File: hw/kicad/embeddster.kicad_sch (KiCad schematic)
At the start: 1 part, among them U1 ESP32-DEVKIT-V1

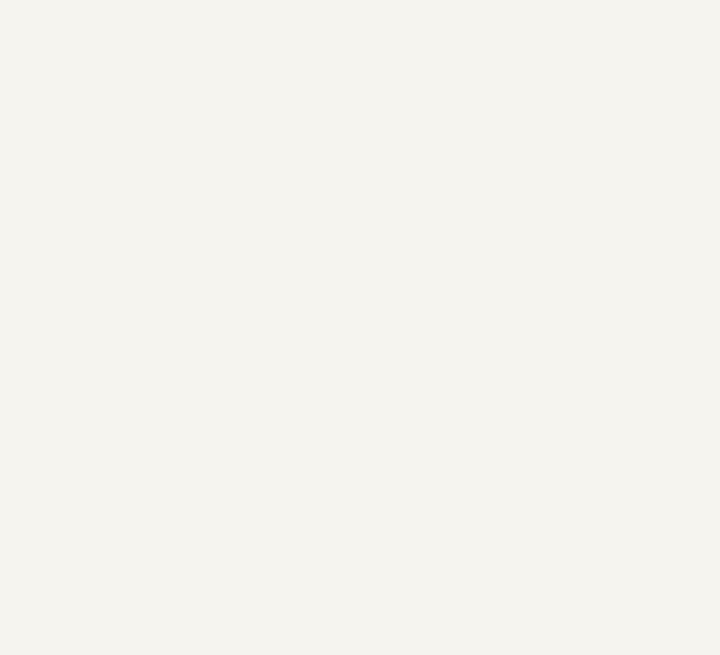
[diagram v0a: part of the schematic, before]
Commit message: Add custom KiCad symbol&footproint for PLACA_CAN_V20190517
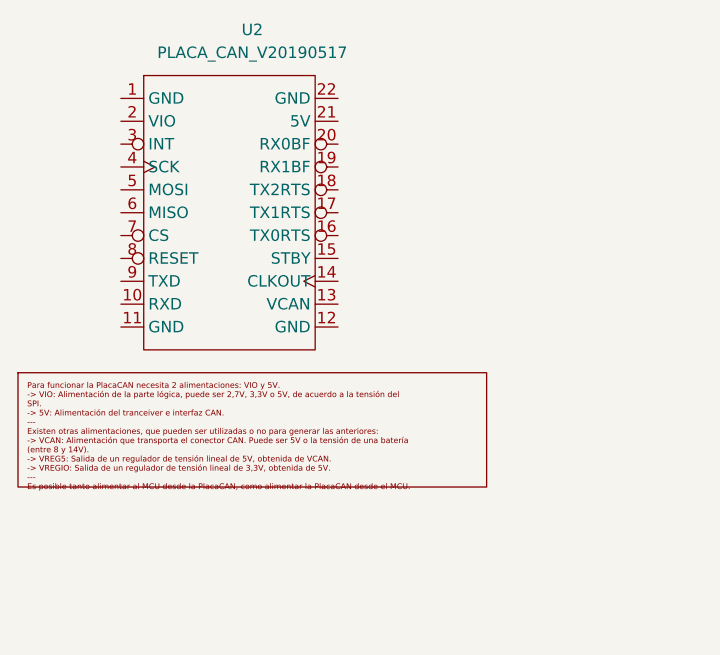
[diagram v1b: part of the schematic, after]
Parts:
- added U2: PLACA_CAN_V20190517, PLACA_CAN_V20190517:PLACA_CAN_V20190517, symbol PLACA_CAN_V20190517:PLACA_CAN_V20190517
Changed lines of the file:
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@@
+		)
+	)
+	(symbol
+		(lib_id "PLACA_CAN_V20190517:PLACA_CAN_V20190517")
+		(at 57.15 27.94 0)
+		(unit 1)
+		(exclude_from_sim no)
+		(in_bom yes)
+		(on_board yes)
+		(dnp no)
+		(fields_autoplaced yes)
+		(property "Reference" "U2"
+			(at 59.055 24.13 0)
+			(effects
+				(font
+					(size 1.27 1.27)
+				)
+			)
+		)
+		(property "Value" "PLACA_CAN_V20190517"
+			(at 59.055 26.67 0)
+			(effects
+				(font
+					(size 1.27 1.27)
+				)
+			)
+		)
+		(property "Footprint" "PLACA_CAN_V20190517:PLACA_CAN_V20190517"
+			(at 57.15 27.94 0)
+			(effects
+				(font
+					(size 1.27 1.27)
+				)
+				(hide yes)
+			)
+		)
+		(property "Datasheet" ""
+			(at 57.15 27.94 0)
+			(effects
+				(font
+					(size 1.27 1.27)
+				)
+				(hide yes)
+			)
+		)
+		(property "Description" ""
+			(at 57.15 27.94 0)
+			(effects
+				(font
+					(size 1.27 1.27)
+				)
+				(hide yes)
+			)
+		)
+		(pin "7"
+		)
+		(pin "20"
+		)
+		(pin "19"
+		)
+		(pin "21"
+		)
+		(pin "2"
+		)
+		(pin "4"
+		)
+		(pin "13"
+		)
+		(pin "22"
+		)
+		(pin "17"
+		)
+		(pin "1"
+		)
+		(pin "5"
+		)
+		(pin "18"
+		)
+		(pin "15"
+		)
+		(pin "16"
+		)
+		(pin "3"
+		)
+		(pin "14"
+		)
+		(pin "6"
+		)
+		(pin "11"
+		)
+		(pin "8"
+		)
+		(pin "10"
+		)
+		(pin "9"
+		)
+		(pin "12"
+		)
+		(instances
+			(project ""
+				(path "/ce96a9a7-c6cd-448d-a47b-e48e55834808"
+					(reference "U2")
+					(unit 1)
+				)
+			)
 		)
 	)

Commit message: sch supporting tp1 & tp2
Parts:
- removed U2: PLACA_CAN_V20190517, PLACA_CAN_V20190517:PLACA_CAN_V20190517, symbol PLACA_CAN_V20190517:PLACA_CAN_V20190517
- added C1, C2: 100n, Capacitor_SMD:C_0805_2012Metric_Pad1.18x1.45mm_HandSolder, symbol Device:C
- added D1, D2, D3, D4, D5, D6: LED, LED_SMD:LED_0805_2012Metric_Pad1.15x1.40mm_HandSolder, symbol Device:LED
- added J1, J2, J3: Conn_01x03_Pin, Connector_PinHeader_2.54mm:PinHeader_1x03_P2.54mm_Vertical, symbol Connector:Conn_01x03_Pin
- added J4: TP1_CONN, Connector_PinSocket_2.54mm:PinSocket_2x09_P2.54mm_Vertical, symbol Connector_Generic:Conn_02x09_Odd_Even
- added JP1, JP2: Jumper_2_Open, TestPoint:TestPoint_2Pads_Pitch2.54mm_Drill0.8mm, symbol Jumper:Jumper_2_Open
- added R1: 680, Resistor_SMD:R_0805_2012Metric_Pad1.20x1.40mm_HandSolder, symbol Device:R
- added R2: 470, Resistor_SMD:R_0805_2012Metric_Pad1.20x1.40mm_HandSolder, symbol Device:R
- added R3, R4, R5, R6: 220, Resistor_SMD:R_0805_2012Metric_Pad1.20x1.40mm_HandSolder, symbol Device:R
- added U1: PLACA_CAN_V20190517, PLACA_CAN_V20190517:PLACA_CAN_V20190517, symbol PLACA_CAN_V20190517:PLACA_CAN_V20190517
- added U3, U4: 74HC595, Package_SO:SOIC-16_3.9x9.9mm_P1.27mm, symbol 74xx:74HC595
- renumbered U1 to U2
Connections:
- net at U2.1 (3V3): now also JP2.1 (A)
- net CAN_MISO: now reaches U2.10 (D19)
- net CAN_MISO: now also U1.6 (MISO)
- net CAN_MOSI: now reaches U2.15 (D23)
- net CAN_MOSI: now also U1.5 (MOSI)
- net GND: now reaches U2.2 (GND), U2.29 (GND)
- net GND: now also C1.1, C2.1, J1.1 (Pin_1), J1.2 (Pin_2), J1.3 (Pin_3), J4.16 (Pin_16), J4.18 (Pin_18), R1.2, R2.2, R3.2, R4.2, R5.2, R6.2, U1.1 (GND), U1.11 (GND), U1.12 (GND), U1.22 (GND), U3.8 (GND), U4.8 (GND)
- net at U2.30 (VIN): now also JP1.2 (B)
- net CAN_nINT: now reaches U2.7 (TX2)
- net CAN_nINT: now also U1.3 (INT)
- net CAN_nCS: now reaches U2.8 (D5)
- net CAN_nCS: now also U1.7 (CS)
- net CAN_SCK: now reaches U2.9 (D18)
- net CAN_SCK: now also U1.4 (SCK)
- new net: D6.2 (A), U4.4 (QE)
- new net: D5.2 (A), U4.5 (QF)
- new net: D4.2 (A), U4.6 (QG)
- new net: D3.2 (A), U4.7 (QH)
- new net: D1.1 (K), R1.1
- new net: D2.1 (K), R2.1
- new net: D6.1 (K), R6.1
- new net: D3.1 (K), R3.1
- new net: D4.1 (K), R4.1
- new net: D5.1 (K), R5.1
- new net +3V3: C1.2, C2.2, D2.2 (A), J3.1 (Pin_1), J3.2 (Pin_2), J3.3 (Pin_3), J4.17 (Pin_17), JP2.2 (B), U3.16 (VCC), U4.16 (VCC)
- new net +5V: D1.2 (A), J2.1 (Pin_1), J2.2 (Pin_2), J2.3 (Pin_3), JP1.1 (A), U1.21 (5V)
- new net 595_LATCH_CLK: U3.12 (RCLK), U4.12 (RCLK)
- new net 595_LINK: U3.9 (QH'), U4.14 (SER)
- new net 595_SHIFT_CLK: U3.11 (SRCLK), U4.11 (SRCLK)
- new net 595_SI: U3.14 (SER)
- new net 595_nOE: U3.13 (~{OE}), U4.13 (~{OE})
- new net 595_nRST: U3.10 (~{SRCLR}), U4.10 (~{SRCLR})
- new net TP1_CSEGA: J4.1 (Pin_1), U3.15 (QA)
- new net TP1_CSEGB: J4.3 (Pin_3), U3.1 (QB)
- new net TP1_CSEGC: J4.5 (Pin_5), U3.2 (QC)
- new net TP1_CSEGD: J4.7 (Pin_7), U3.3 (QD)
- new net TP1_CSEGDP: J4.15 (Pin_15), U3.7 (QH)
- new net TP1_CSEGE: J4.9 (Pin_9), U3.4 (QE)
- new net TP1_CSEGF: J4.11 (Pin_11), U3.5 (QF)
- new net TP1_CSEGG: J4.13 (Pin_13), U3.6 (QG)
- new net TP1_RCHA: J4.6 (Pin_6)
- new net TP1_RCHB: J4.8 (Pin_8)
- new net TP1_RSWITCH: J4.10 (Pin_10)
- new net TP1_SEL0: J4.2 (Pin_2), U4.15 (QA)
- new net TP1_SEL1: J4.4 (Pin_4), U4.1 (QB)
- new net TP1_STATUS0: J4.12 (Pin_12), U4.2 (QC)
- new net TP1_STATUS1: J4.14 (Pin_14), U4.3 (QD)
- no-connect marks 0 -> 13
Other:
- moved on the sheet: U2

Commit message: pcb ready for fab
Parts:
- added C3, C4, C5: 100n, Capacitor_SMD:C_0805_2012Metric_Pad1.18x1.45mm_HandSolder, symbol Device:C
- added J5, J6, J7: Conn_01x05_Socket, Connector_PinSocket_2.54mm:PinSocket_1x05_P2.54mm_Vertical, symbol Connector:Conn_01x05_Socket
- added R7, R8: 10k, Resistor_SMD:R_0805_2012Metric_Pad1.20x1.40mm_HandSolder, symbol Device:R
- D1: footprint LED_SMD:LED_0805_2012Metric_Pad1.15x1.40mm_HandSolder -> LED_THT:LED_D3.0mm
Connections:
- net +3V3: now also U1.2 (VIO), C3.2, R7.1, R8.1
- net 595_LATCH_CLK: now also U2.22 (D33)
- net 595_SHIFT_CLK: now also U2.25 (D27)
- net 595_SI: now also U2.21 (D32)
- net 595_nOE: now also U2.23 (D25), R7.2
- net 595_nRST: now also U2.24 (D26), R8.2
- net GND: now also C3.1, C4.1, C5.1, J5.1 (Pin_1), J5.2 (Pin_2), J5.3 (Pin_3), J5.4 (Pin_4), J5.5 (Pin_5), J6.1 (Pin_1), J6.2 (Pin_2), J6.3 (Pin_3), J6.4 (Pin_4), J6.5 (Pin_5), J7.1 (Pin_1), J7.2 (Pin_2), J7.3 (Pin_3), J7.4 (Pin_4), J7.5 (Pin_5)
- net TP1_CSEGA: now also U3.7 (QH); no longer U3.15 (QA)
- net TP1_CSEGB: now also U3.6 (QG); no longer U3.1 (QB)
- net TP1_CSEGC: now also U3.5 (QF); no longer U3.2 (QC)
- net TP1_CSEGD: now also U3.4 (QE); no longer U3.3 (QD)
- net TP1_CSEGDP: now also U3.15 (QA); no longer U3.7 (QH)
- net TP1_CSEGE: now also U3.3 (QD); no longer U3.4 (QE)
- net TP1_CSEGF: now also U3.2 (QC); no longer U3.5 (QF)
- net TP1_CSEGG: now also U3.1 (QB); no longer U3.6 (QG)
- net TP1_RCHA: now also U2.6 (RX2)
- net TP1_RCHB: now also U2.11 (D21)
- net TP1_RSWITCH: now also U2.14 (D22)
- net at JP2.1 (A), U2.1 (3V3): now also C5.2
- net at JP1.2 (B), U2.30 (VIN): now also C4.2
- no-connect marks 13 -> 12
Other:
- note added: "Output disabled by default"
- note added: "Quantum Standoffs"
- title: (none) -> Embeddster PCB

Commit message: Add 4th quantum standoff to PCB, ground plane adjustments
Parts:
- added J8: Conn_01x05_Socket, Connector_PinSocket_2.54mm:PinSocket_1x05_P2.54mm_Vertical, symbol Connector:Conn_01x05_Socket
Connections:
- net GND: now also J8.1 (Pin_1), J8.2 (Pin_2), J8.3 (Pin_3), J8.4 (Pin_4), J8.5 (Pin_5)
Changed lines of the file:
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@@
 	)
 	(junction
+		(at 184.15 85.09)
+		(diameter 0)
+		(color 0 0 0 0)
+	)
+	(junction
 		(at 151.13 30.48)
 		(diameter 0)
@@
 	)
 	(junction
+		(at 189.23 85.09)
+		(diameter 0)
+		(color 0 0 0 0)
+	)
+	(junction
 		(at 156.21 101.6)
 		(diameter 0)
@@
 	)
 	(junction
+		(at 181.61 85.09)
+		(diameter 0)
+		(color 0 0 0 0)
+	)
+	(junction
 		(at 251.46 43.18)
 		(diameter 0)
@@
 	)
 	(junction
+		(at 179.07 85.09)
+		(diameter 0)
+		(color 0 0 0 0)
+	)
+	(junction
 		(at 189.23 101.6)
 		(diameter 0)
@@
 	)
 	(junction
+		(at 186.69 85.09)
+		(diameter 0)
+		(color 0 0 0 0)
+	)
+	(junction
 		(at 177.8 85.09)
 		(diameter 0)
@@
 	(wire
 		(pts
-			(xy 189.23 85.09) (xy 177.8 85.09)
+			(xy 189.23 85.09) (xy 186.69 85.09)
 		)
 		(stroke
@@
 	(wire
 		(pts
+			(xy 186.69 85.09) (xy 184.15 85.09)
+		)
+		(stroke
+			(width 0)
+			(type default)
+		)
+	)
+	(wire
+		(pts
 			(xy 34.29 48.26) (xy 45.72 48.26)
 		)
@@
 	(wire
 		(pts
+			(xy 184.15 85.09) (xy 181.61 85.09)
+		)
+		(stroke
+			(width 0)
+			(type default)
+		)
+	)
+	(wire
+		(pts
 			(xy 35.56 135.89) (xy 35.56 149.86)
 		)
@@
 	(wire
 		(pts
+			(xy 179.07 85.09) (xy 177.8 85.09)
+		)
+		(stroke
+			(width 0)
+			(type default)
+		)
+	)
+	(wire
+		(pts
 			(xy 35.56 107.95) (xy 43.18 107.95)
 		)
@@
 	(wire
 		(pts
+			(xy 181.61 85.09) (xy 179.07 85.09)
+		)
+		(stroke
+			(width 0)
+			(type default)
+		)
+	)
+	(wire
+		(pts
 			(xy 172.72 85.09) (xy 170.18 85.09)
 		)
@@
 					(unit 1)
 				)
+			)
+		)
+	)
+	(symbol
+		(lib_id "Connector:Conn_01x05_Socket")
+		(at 184.15 80.01 90)
+		(unit 1)
+		(exclude_from_sim no)
+		(in_bom yes)
+		(on_board yes)
+		(dnp no)
+		(fields_autoplaced yes)
+		(property "Reference" "J8"
+			(at 184.15 74.93 90)
+			(effects
+				(font
+					(size 1.27 1.27)
+				)
+			)
+		)
+		(property "Value" "Conn_01x05_Socket"
+			(at 184.15 77.47 90)
+			(effects
+				(font
+					(size 1.27 1.27)
+				)
+			)
+		)
+		(property "Footprint" "Connector_PinSocket_2.54mm:PinSocket_1x05_P2.54mm_Vertical"
+			(at 184.15 80.01 0)
+			(effects
+				(font
+					(size 1.27 1.27)
+				)
+				(hide yes)
+			)
+		)
+		(property "Datasheet" "~"
+			(at 184.15 80.01 0)
+			(effects
+				(font
+					(size 1.27 1.27)
+				)
+				(hide yes)
+			)
+		)
+		(property "Description" "Generic connector, single row, 01x05, script generated"
+			(at 184.15 80.01 0)
+			(effects
+				(font
+					(size 1.27 1.27)
+				)
+				(hide yes)
+			)
+		)
+		(pin "2"
+		)
+		(pin "1"
+		)
+		(pin "3"
+		)
+		(pin "5"
+		)
+		(pin "4"
+		)
+		(instances
+			(project "embeddster"
+				(path "/ce96a9a7-c6cd-448d-a47b-e48e55834808"
+					(reference "J8")
+					(unit 1)
+				)

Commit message: Add a WS2812B cell
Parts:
- added C6: 100n, Capacitor_SMD:C_0805_2012Metric_Pad1.18x1.45mm_HandSolder, symbol Device:C
- added D7: WS2812B, LED_SMD:LED_WS2812B_PLCC4_5.0x5.0mm_P3.2mm, symbol LED:WS2812B
- added R9: 470, Resistor_SMD:R_0805_2012Metric_Pad1.20x1.40mm_HandSolder, symbol Device:R
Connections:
- net +5V: now also C6.2, D7.1 (VDD)
- net GND: now also C6.1, D7.3 (VSS)
- net TP1_RCHA: now also U2.5 (D4); no longer U2.6 (RX2)
- net TP1_RCHB: now also U2.6 (RX2); no longer U2.11 (D21)
- new net: D7.4 (DIN), R9.2
- new net NPXL: R9.1, U2.11 (D21)
- no-connect marks 12 -> 13
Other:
- moved on the sheet: D1, D2, R1, R2
